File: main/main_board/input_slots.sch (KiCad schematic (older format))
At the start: 16 parts, among them J7 SCKB, J8 SCKA, J9 MCLK, U14 74LVC541A, U15 FIN1047, U16 FIN1047, U17 FIN1047

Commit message: Mostly work on hooking in the Microzed using kipart symbols and a footprint. Also added 2.5V VCCIO regulator.
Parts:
- removed J9: MCLK, Connector_Coaxial:MMCX_Molex_73415-1471_Vertical, symbol Connector:Conn_Coaxial
- removed R42: 1K, Resistor_SMD:R_0603_1608Metric, symbol Device:R_US
- added C54: 100nF, Capacitor_SMD:C_0603_1608Metric, symbol Device:C_Small
- added R10, R11, R9: 100, Resistor_SMD:R_0603_1608Metric, symbol Device:R_US
- added RN1: 33, Resistor_SMD:R_Array_Convex_4x0603, symbol Device:R_Pack04
- added U5: DS90LV048, Package_SO:TSSOP-16_4.4x5mm_P0.65mm, symbol ilemt_input:FIN1048
- added X1: MicroZed, main_board:Microzed, symbol microzed:MicroZed
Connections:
- net labels added: FPGA_SYSCLK+, FPGA_SYSCLK-, MCLK_ENA
- net labels removed: CARDSEL0, CARDSEL1, CARDSEL2, CARDSEL3, FPGA_SYNC, MCLK_JACK, SCKA, SCKB
- wire segments 153 -> 301
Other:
- note added: "B038\nB041"
- moved on the sheet: C48, C49, C50, C51, C52, J7, J8, R40, R41, RN4, U14, U15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

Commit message: Updated for new microzed pin mapping scheme.
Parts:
- X1: value MicroZed -> microzed; symbol microzed:MicroZed -> microzed:microzed
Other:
- note removed: "B038\nB041"
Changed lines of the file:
@@
 	4600 12550 5875 12550
 $Comp
-L microzed:MicroZed X1
+L microzed:microzed X1
 U 2 1 5F0A97DA
 P 17800 1950
 AR Path="/5F0A97DA" Ref="X1"  Part="2"
-AR Path="/5E525FFE/5F0A97DA" Ref="X1"  Part="2"
-F 0 "X1" H 18000 2200 60  0000 L CNN
-F 1 "MicroZed" H 18000 2100 60  0000 L CNN
+AR Path="/5E525FFE/5F0A97DA" Ref="M1"  Part="2"
+F 0 "M1" H 18000 2200 60  0000 L CNN
+F 1 "microzed" H 18000 2100 60  0000 L CNN
 F 2 "main_board:Microzed" H 18000 2000 60  0001 L CNN
 F 3 "" H 18000 1800 60  0001 L CNN
@@
 	15750 1350 15750 1900
 $Comp
-L microzed:MicroZed X1
+L microzed:microzed X1
 U 1 1 5F1431B2
 P 2700 11450
 AR Path="/5F1431B2" Ref="X1"  Part="1"
-AR Path="/5E525FFE/5F1431B2" Ref="X1"  Part="1"
-F 0 "X1" H 2900 11700 60  0000 L CNN
-F 1 "MicroZed" H 2900 11600 60  0000 L CNN
+AR Path="/5E525FFE/5F1431B2" Ref="M1"  Part="1"
+F 0 "M1" H 2900 11700 60  0000 L CNN
+F 1 "microzed" H 2900 11600 60  0000 L CNN
 F 2 "main_board:Microzed" H 2900 11500 60  0001 L CNN
 F 3 "" H 2900 11300 60  0001 L CNN
@@
 	4400 7900 6350 7900
 $Comp
-L microzed:MicroZed X1
+L microzed:microzed X1
 U 3 1 5F159E9E
 P 17800 3600
 AR Path="/5F159E9E" Ref="X1"  Part="3"
-AR Path="/5E525FFE/5F159E9E" Ref="X1"  Part="3"
-F 0 "X1" H 18000 3850 60  0000 L CNN
-F 1 "MicroZed" H 18000 3750 60  0000 L CNN
+AR Path="/5E525FFE/5F159E9E" Ref="M1"  Part="3"
+F 0 "M1" H 18000 3850 60  0000 L CNN
+F 1 "microzed" H 18000 3750 60  0000 L CNN
 F 2 "main_board:Microzed" H 18000 3650 60  0001 L CNN
 F 3 "" H 18000 3450 60  0001 L CNN
@@
 	17750 3500 17750 3600
 $Comp
-L microzed:MicroZed X1
+L microzed:microzed X1
 U 4 1 5F1854CB
 P 17800 5300
 AR Path="/5F1854CB" Ref="X1"  Part="4"
-AR Path="/5E525FFE/5F1854CB" Ref="X1"  Part="4"
-F 0 "X1" H 18000 5550 60  0000 L CNN
-F 1 "MicroZed" H 18000 5450 60  0000 L CNN
+AR Path="/5E525FFE/5F1854CB" Ref="M1"  Part="4"
+F 0 "M1" H 18000 5550 60  0000 L CNN
+F 1 "microzed" H 18000 5450 60  0000 L CNN
 F 2 "main_board:Microzed" H 18000 5350 60  0001 L CNN
 F 3 "" H 18000 5150 60  0001 L CNN
@@
 	17750 5300 17800 5300
 $Comp
-L microzed:MicroZed X1
+L microzed:microzed X1
 U 5 1 5F209C7E
 P 17800 7050
 AR Path="/5F209C7E" Ref="X1"  Part="5"
-AR Path="/5E525FFE/5F209C7E" Ref="X1"  Part="5"
-F 0 "X1" H 18000 7300 60  0000 L CNN
-F 1 "MicroZed" H 18000 7200 60  0000 L CNN
+AR Path="/5E525FFE/5F209C7E" Ref="M1"  Part="5"
+F 0 "M1" H 18000 7300 60  0000 L CNN
+F 1 "microzed" H 18000 7200 60  0000 L CNN
 F 2 "main_board:Microzed" H 18000 7100 60  0001 L CNN
 F 3 "" H 18000 6900 60  0001 L CNN
@@
 Wire Wire Line
 	2600 11650 2700 11650
-Text Notes 19600 5400 0    50   ~ 0
-B038\nB041
 $EndSCHEMATC

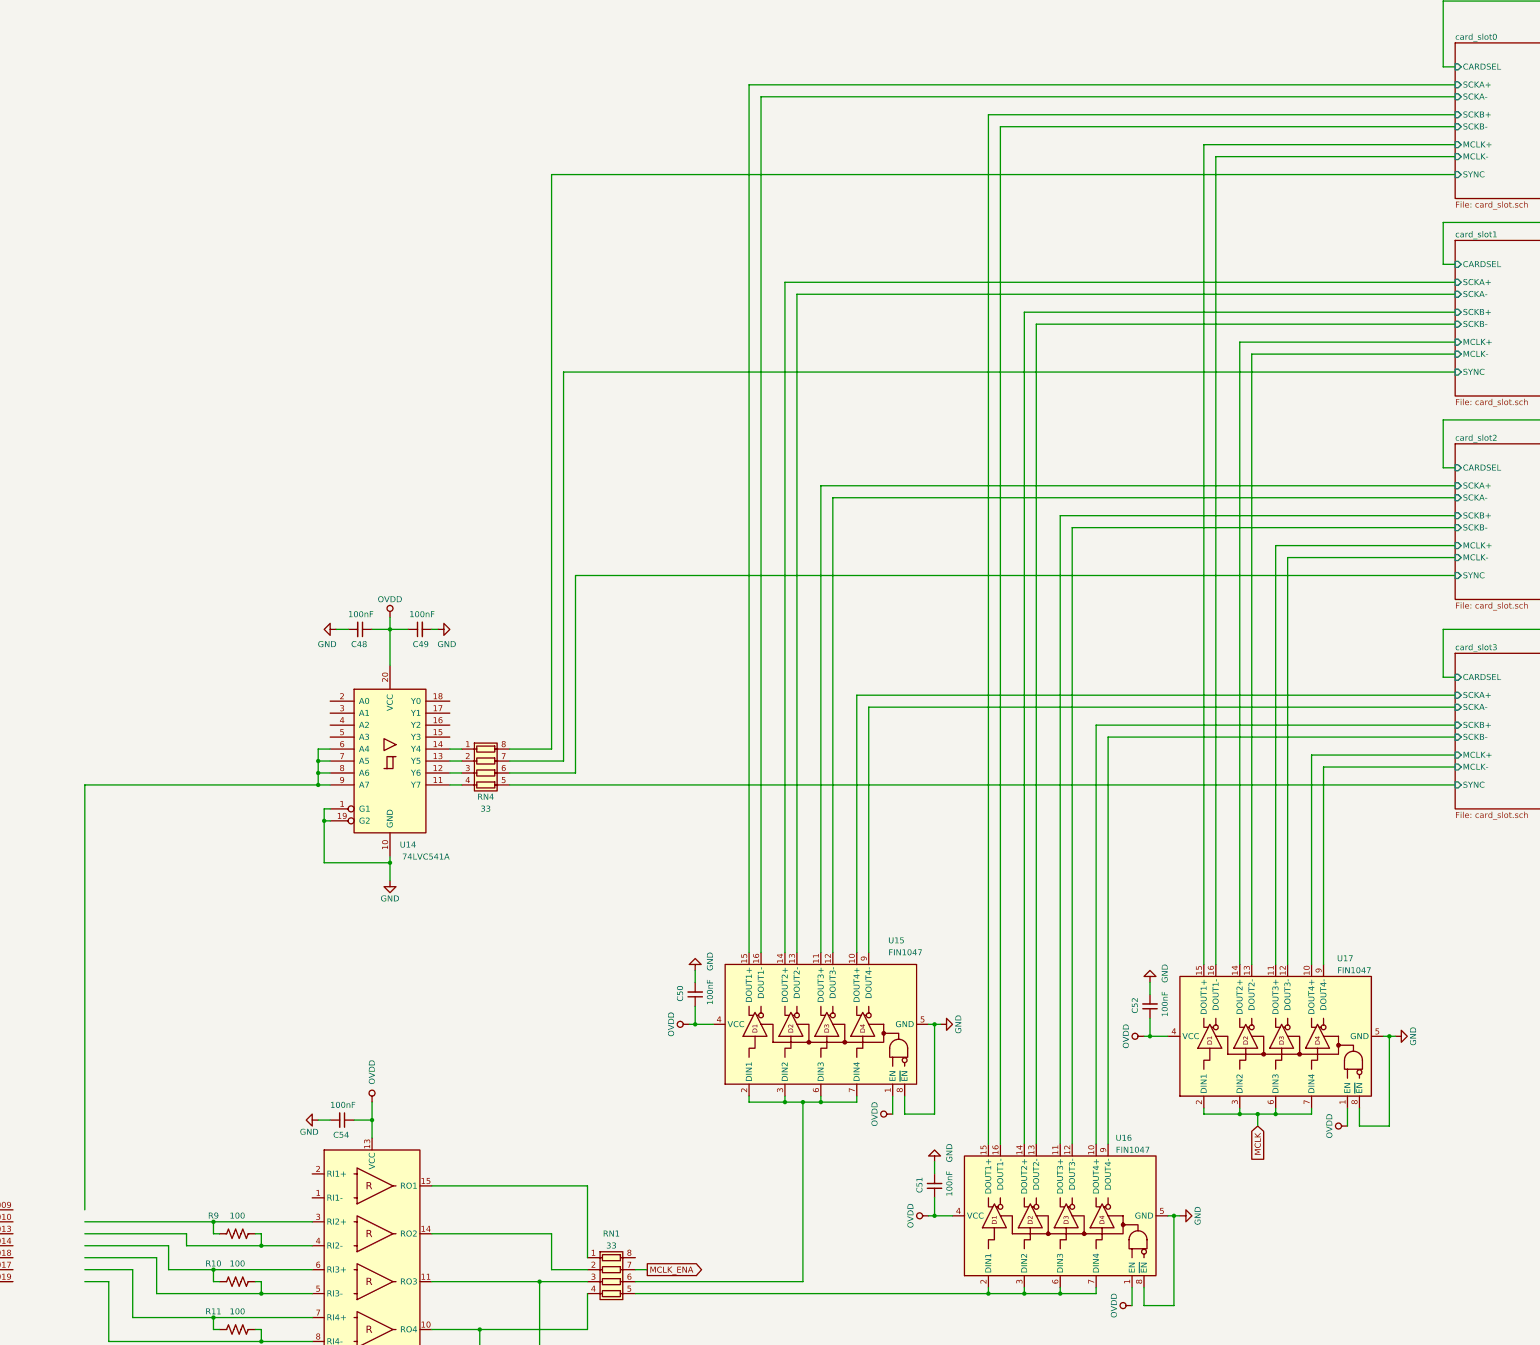
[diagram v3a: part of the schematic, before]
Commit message: Schematic is mostly complete (except for BIST DACs), and passes ERC.  Rough placement of components on PCB.
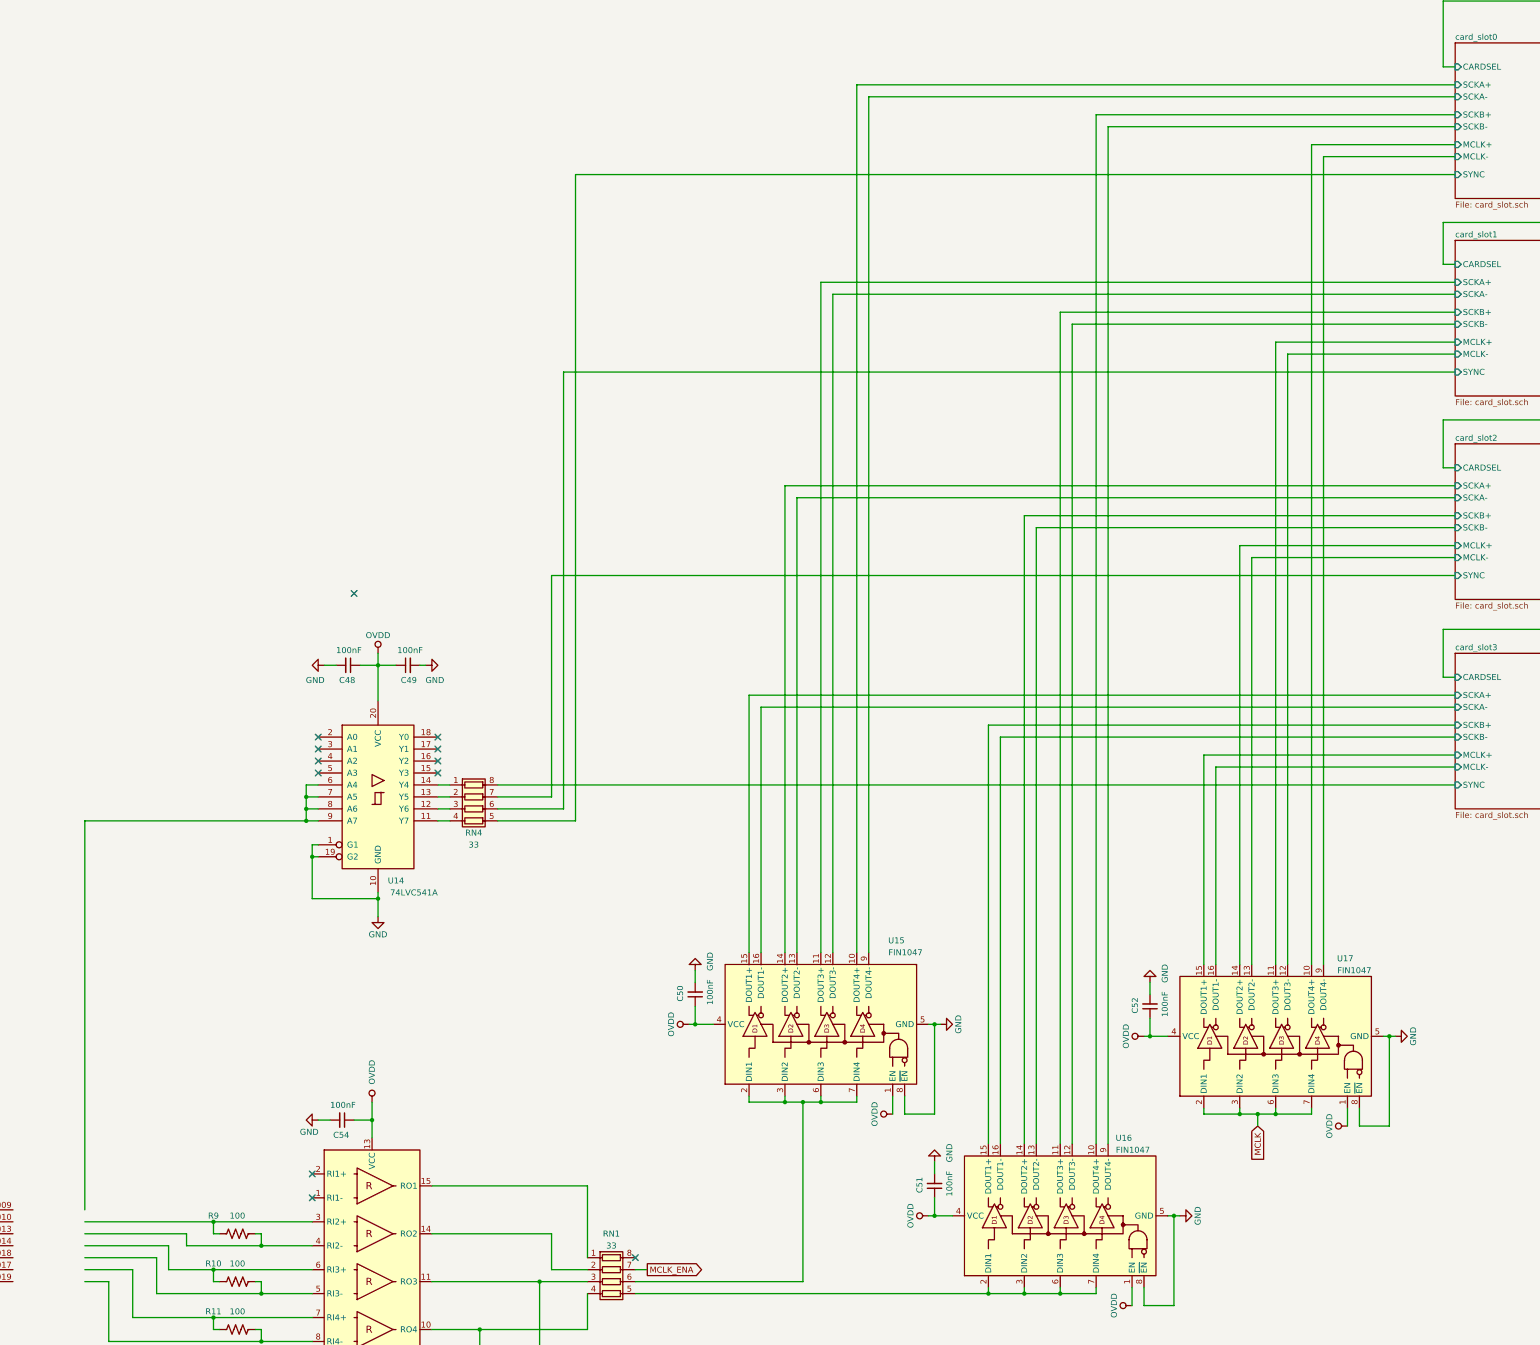
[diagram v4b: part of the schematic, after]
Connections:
- no-connect marks 0 -> 12
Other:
- moved on the sheet: C48, C49, RN4, U14

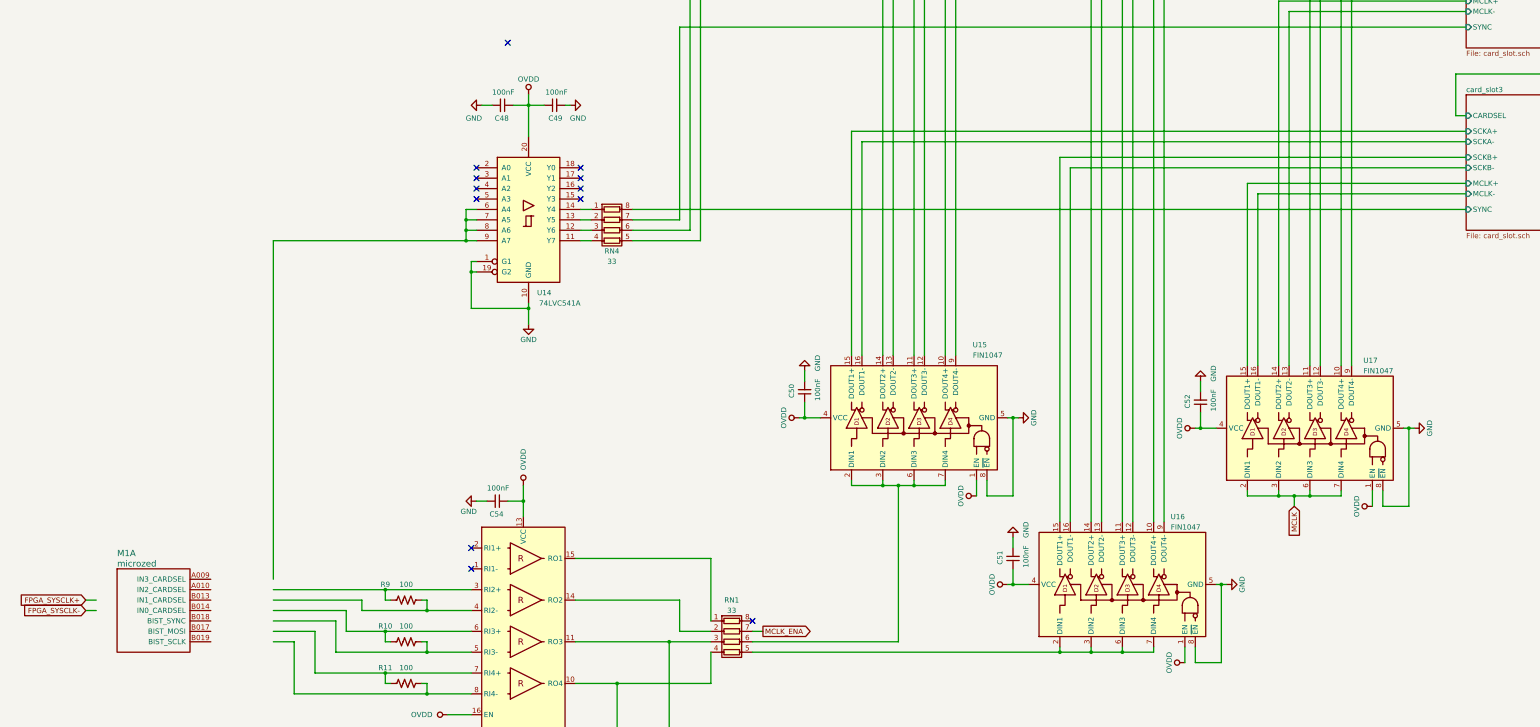
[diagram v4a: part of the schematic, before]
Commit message: Mechanical feature layout on main board (edge connector and mount hole locations).  Added some dimension callouts to the input board. Tweaked grounding on main board schematic.  Chassis ground is not connected to main board ground except via an optional capacitor.  Chassis ground comes in on the power connector. Added BIST DAC, including additions to power.sch and input_slots.sch.
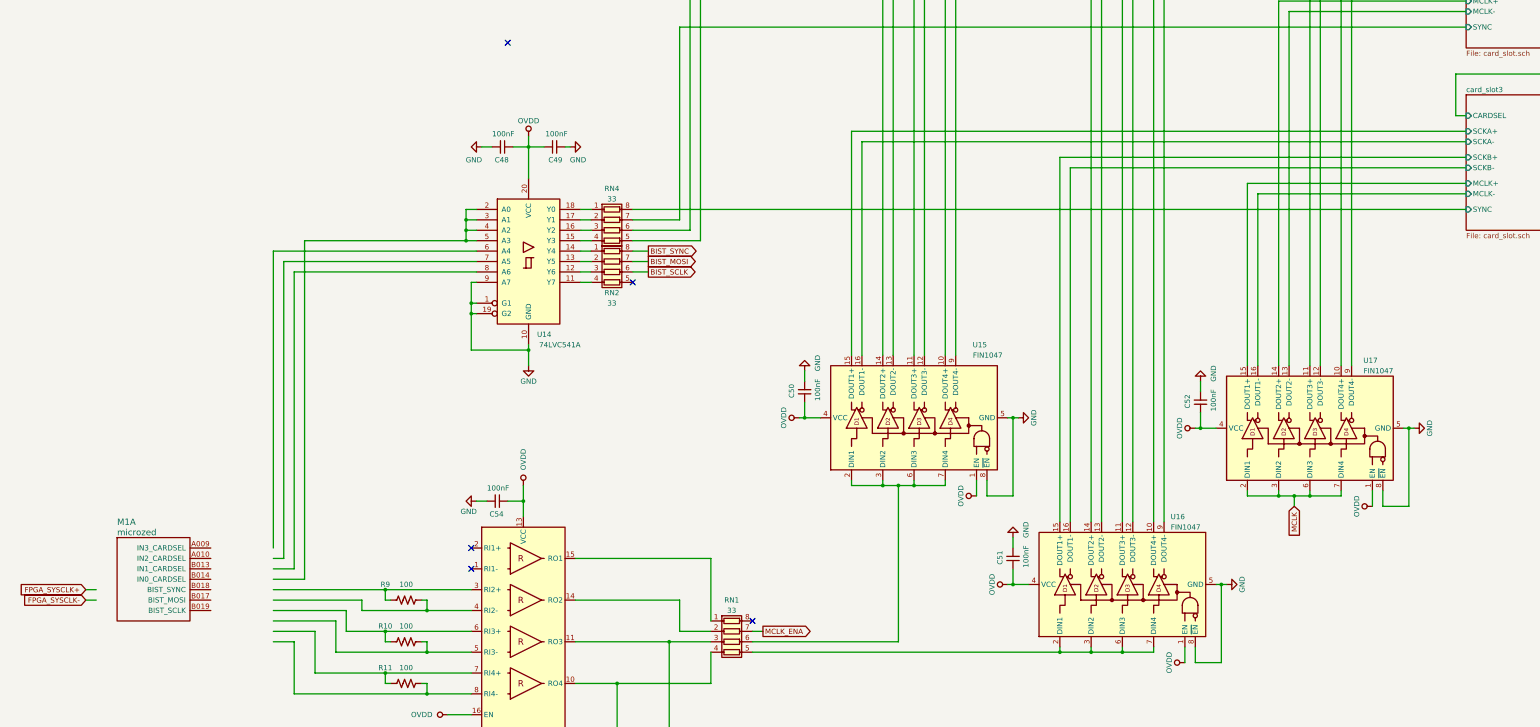
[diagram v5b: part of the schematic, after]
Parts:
- added RN2: 33, Resistor_SMD:R_Array_Convex_4x0603, symbol Device:R_Pack04
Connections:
- net labels added: BIST_MOSI, BIST_SCLK, BIST_SYNC
- wire segments 301 -> 319
- no-connect marks 12 -> 5
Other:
- moved on the sheet: C48, C49, M1A, U14

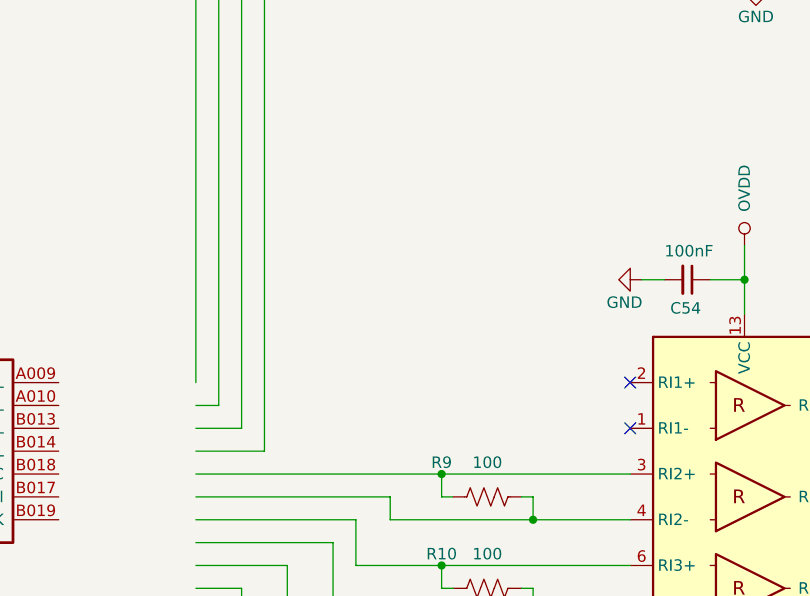
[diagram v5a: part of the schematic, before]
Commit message: Mostly work on main board layout. Aligned things on mm grid for easier routing, moved things around to create routing area. Neatened up component groups onto the grid. Parts of the routing plan are now drawn on the PCB.  See also notebook.txt. Reduced pad size of the PCIE connector, tweaked design rule clearances. Minor schematic tweaks.
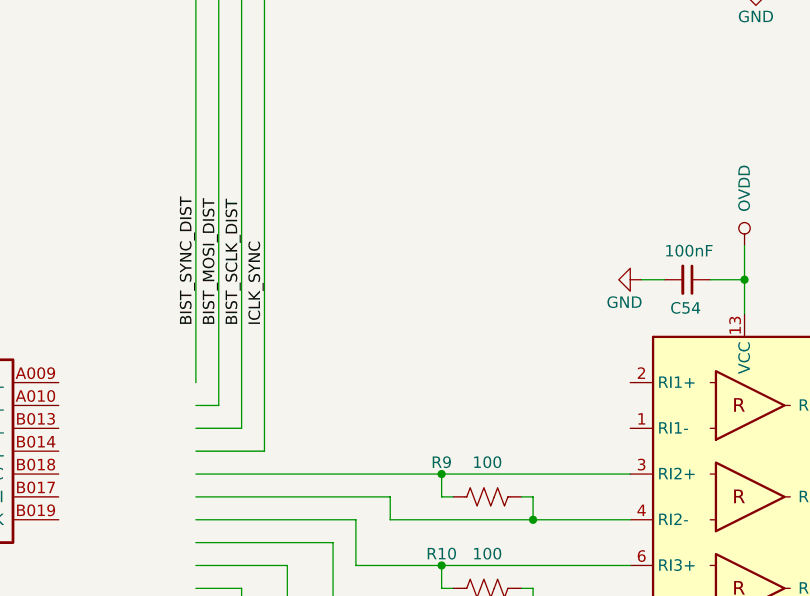
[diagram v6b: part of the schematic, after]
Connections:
- net labels added: BIST_MOSI_DIST, BIST_SCLK_DIST, BIST_SYNC_DIST, ICLK_SYNC
- no-connect marks 5 -> 3
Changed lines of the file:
@@
 	2600 11550 2700 11550
 NoConn ~ 9000 11850
-NoConn ~ 6300 11350
-NoConn ~ 6300 11150
 NoConn ~ 6650 6300
 Wire Wire Line
@@
 	8500 2800 8500 8200
 Wire Wire Line
-	4500 11250 4400 11250
-Wire Wire Line
 	6350 8500 4600 8500
 Wire Wire Line
@@
 	4400 8300 4400 11150
 Wire Wire Line
-	4500 8400 4500 11250
-Wire Wire Line
 	4600 8500 4600 11350
 Wire Wire Line
@@
 Wire Wire Line
 	4500 8400 6350 8400
+Text Label 4700 10900 1    50   ~ 0
+ICLK_SYNC
+Text Label 4600 10900 1    50   ~ 0
+BIST_SCLK_DIST
+Text Label 4400 10900 1    50   ~ 0
+BIST_SYNC_DIST
+Wire Wire Line
+	4500 11250 4400 11250
+Text Label 4500 10900 1    50   ~ 0
+BIST_MOSI_DIST
+Wire Wire Line
+	4500 8400 4500 11250
 $EndSCHEMATC
